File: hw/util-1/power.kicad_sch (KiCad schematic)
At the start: 17 parts, among them J1 Conn_01x02, J2 Conn_01x03, U2 NCP1117-5.0_SOT223, U3 NCP1117-3.3_SOT223

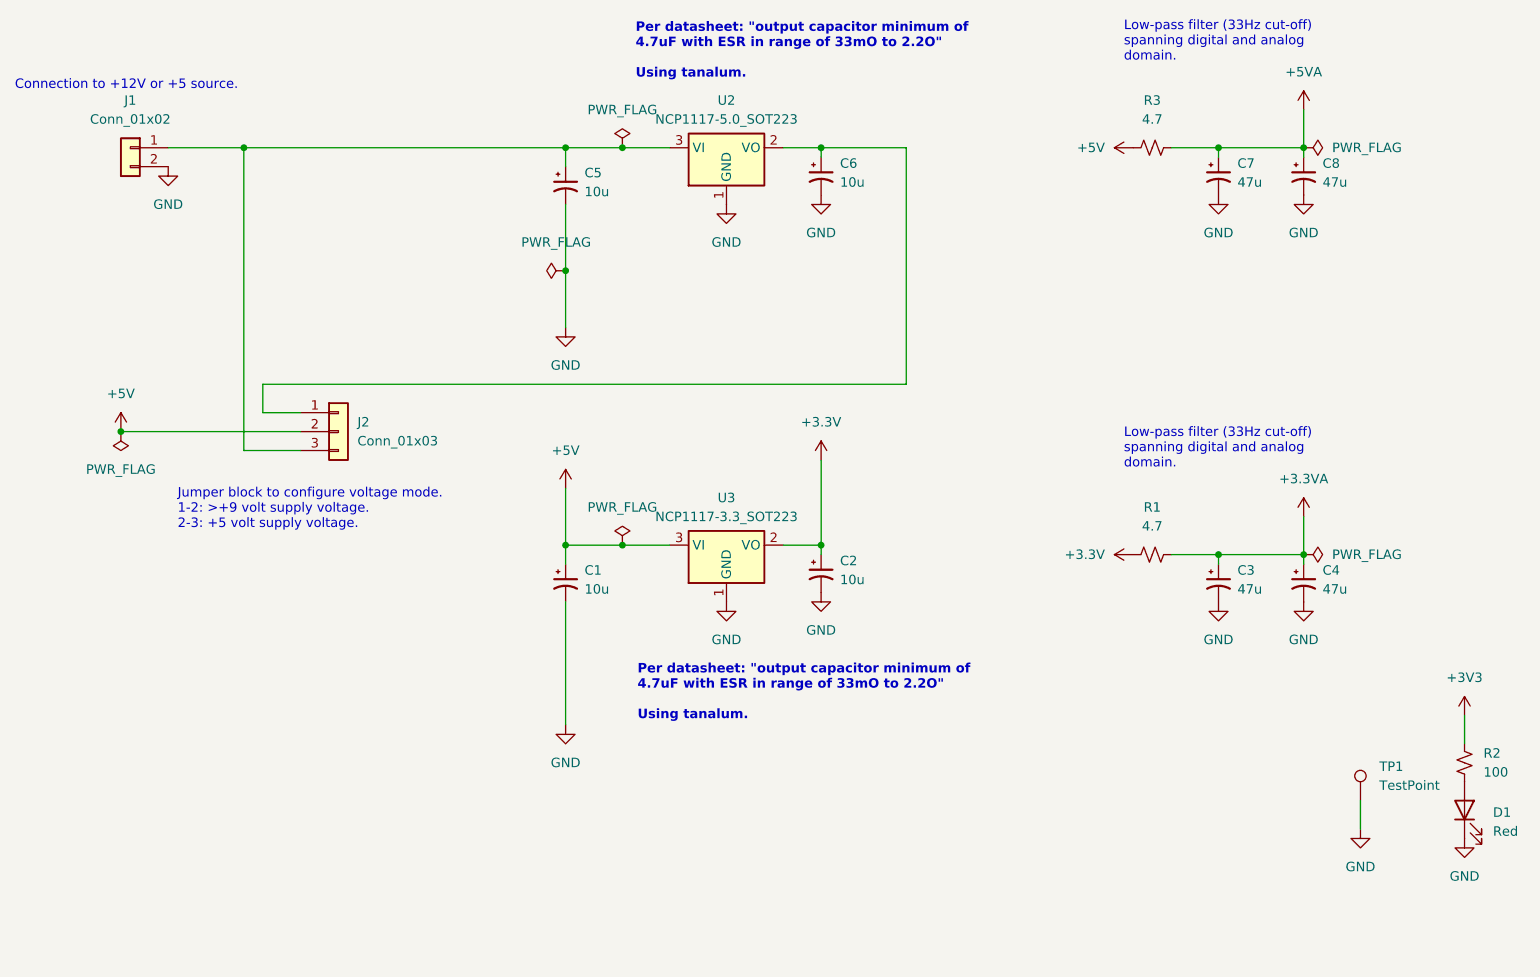
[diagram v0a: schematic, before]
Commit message: Initial version of PCB layout
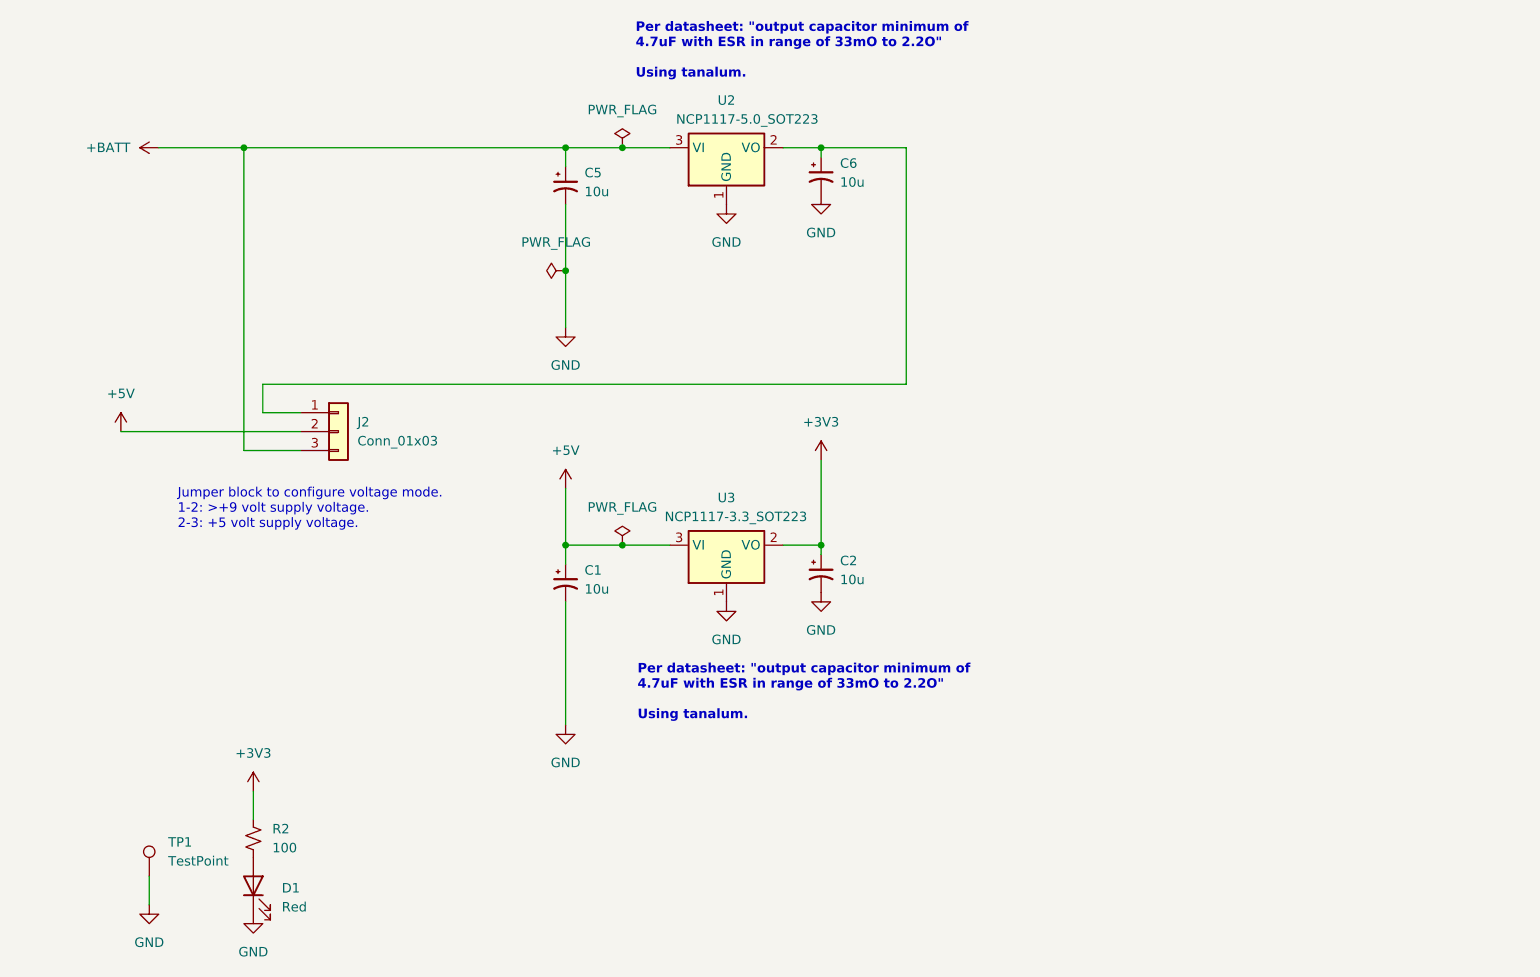
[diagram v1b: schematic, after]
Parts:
- removed C3, C4, C7, C8: 47u, bruce-footprints:CPOL_0805_2012Metric_Pad1.18x1.45mm_HandSolder, symbol Device:C_Polarized_Small_US
- removed J1: Conn_01x02, symbol Connector_Generic:Conn_01x02
- removed R1, R3: 4.7, Resistor_SMD:R_0805_2012Metric_Pad1.20x1.40mm_HandSolder, symbol Device:R_Small_US
- J2: footprint (none) -> Connector_PinHeader_2.54mm:PinHeader_1x03_P2.54mm_Vertical
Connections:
- net +3.3V is gone; now on net +3V3: C2.1, U3.2 (VO)
- net +BATT: now reaches C5.1, J2.3 (Pin_3), U2.3 (VI)
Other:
- note removed: "Connection to +12V or +5 source."
- note removed: "Low-pass filter (33Hz cut-off) spanning digital and analog domain."
- company: (none) -> Bruce MacKinnon KC1FSZ
- title: (none) -> Utility Board 1
- moved on the sheet: D1, R2, TP1
